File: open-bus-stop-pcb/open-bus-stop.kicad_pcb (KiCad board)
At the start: 2 copper layers, 62.5 x 42.5 mm, 41 parts, among them J1 Conn_01x04_Pin, J2 Conn_01x02_Pin, J3 Conn_01x02, J5 Conn_01x02, P1 USB_C_Plug_USB2.0, SW2 SW_Push, SW4 SW_Push, U1 ESP32-C3-MINI-1, U2 DS3231M, U3 BQ24074RGT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

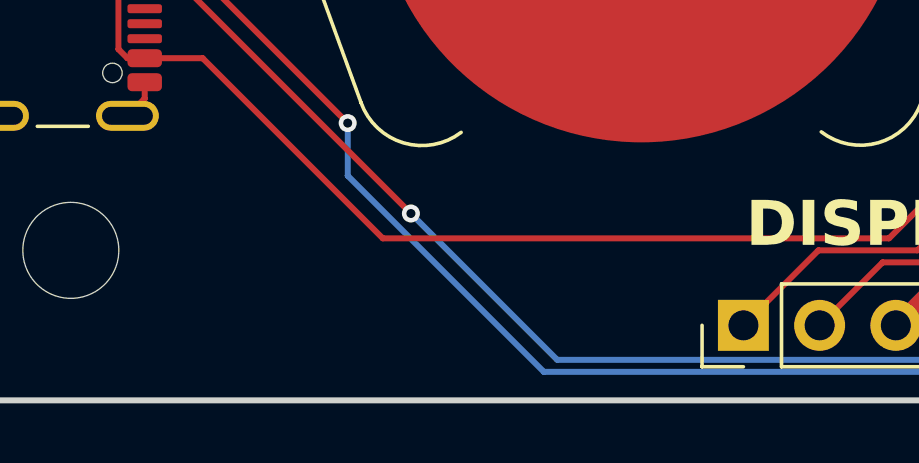
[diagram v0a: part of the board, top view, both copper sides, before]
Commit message: (WIP) swapping RTCs and Display to decrease BOM cost
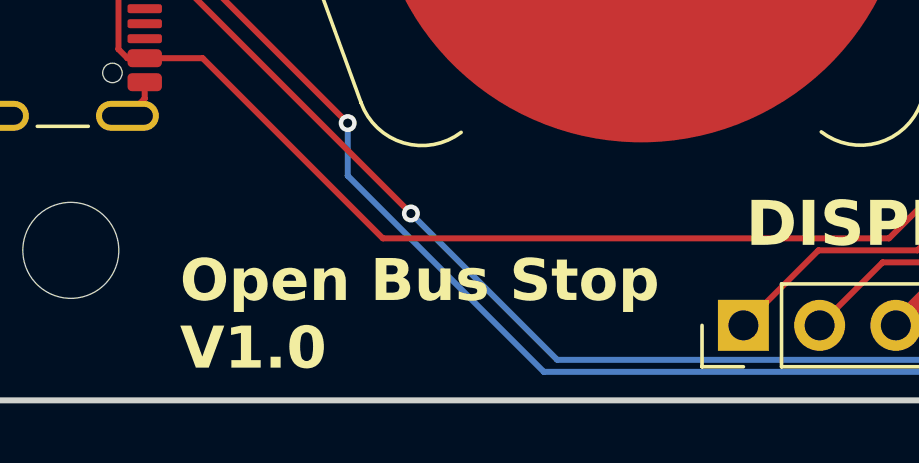
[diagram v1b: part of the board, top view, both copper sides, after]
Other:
- board text added: "Open Bus Stop V1.0"
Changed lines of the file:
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@@
+		)
+	)
+	(gr_text "Open Bus Stop\nV1.0"
+		(at 156.139149 99.079806 0)
+		(layer "F.SilkS")
+		(effects
+			(font
+				(size 1.4 1.4)
+				(thickness 0.3)
+				(bold yes)
+			)
+			(justify left bottom)
 		)
 	)
